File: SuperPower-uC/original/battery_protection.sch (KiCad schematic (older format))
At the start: 0 parts

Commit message: Add "Battery Module" sheet components
+ components libraries
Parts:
- added BT2: 3,7V_18650_LiPo_Bat._Holder, symbol Device:Battery_Cell
- added C8: 100nF, symbol Device:C
- added J9: JST_XH_3A, symbol Connector:Conn_01x02_Male
- added Q6: DMG6968UTS, Package_SO:TSSOP-8_4.4x3mm_P0.65mm, symbol Transistor_FET:DMG6968UTS
- added R21: 330Ohm, symbol Device:R_US
- added R22: 2.7kOhm, symbol Device:R_US
- added U4: AP9101CK6_v2, Package_TO_SOT_SMD:SOT-23-6, symbol Battery_Management:AP9101CK6_v2
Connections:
- net labels added: +BATT, -BATT, GND
- wire segments 0 -> 39
- no-connect marks 0 -> 2
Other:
- note added: "AP9101CK6 Chip price range from Mouser (10/2020) :\n$0.44-0.44 @qt=1\n$0.33-0.33 @qt=10\n$0.17-0.17 @qt=100"
- note added: "AVAILABLE Chips for Lithium-Ion / LiPo or LiFeFO4"
- note added: "Chinese Chip price range from LCSC (10/2020) :\n$0.075-0.115 @qt=10\n$0.054-0.087 @qt=100"
- note added: "Chip + Dual N-Mosfet Version"
- note added: "Compatible pin to pin SOT23-6 ICs List :\n- AP9101CK6 (x65)\n- DW01x (x7)\n- FS312F-G (x1)\n- FS326x (x4)\n- HY2112-xx (x6) for LiFePO4 ONLY\n- HY2113-xxxx (x25) for Lithium ONLY"
- note added: "Compatible pin to pin TSSOP-8 Dual MOSFET List :\n- DMN2019UTS (with ESD Protection diodes)\n- DMG6968UTS (with ESD Protection diodes)\n- FS8205A"
- note added: "Components Price Range"
- note added: "LiFePO4 SOT23-6 ICs List :\n- AP9101CK6-CPTRG1 (3,65V)\n- AP9101CK6-ASTRG1 (3,80V)\n- HY2112-AB (3,75V)\n- HY2112-BB (3,75V)\n- HY2112-CB (3,75V)"
- note added: "LiFePO4 chip list"
- note added: "MOSFET price range from LCSC (10/2020) :\n$0.174-0.357 @qt=1\n$0.128-0.347 @qt=10\n$0.111-0.333 @qt=100"
- note added: "SOT23-6 Package"
- note added: "TSSOP-8 Package"

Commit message: Replace the Dual N-MOSFET by a cheaper version
Replace DMG6968UTS by DMN2019UTS
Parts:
- removed Q6: DMG6968UTS, Package_SO:TSSOP-8_4.4x3mm_P0.65mm, symbol Transistor_FET:DMG6968UTS
- added Q?: DMN2019UTS, Package_SO:TSSOP-8_4.4x3mm_P0.65mm, symbol dmn2019uts:DMN2019UTS
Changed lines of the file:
@@
 	-1   0    0    1
-$EndComp
-$Comp
-L Transistor_FET:DMG6968UTS Q6
-U 1 1 5F79C65E
-P 2650 5200
-F 0 "Q6" H 3094 5196 50  0000 L CNN
-F 1 "DMG6968UTS" H 3094 5105 50  0000 L CNN
-F 2 "Package_SO:TSSOP-8_4.4x3mm_P0.65mm" H 2850 5450 50  0001 L CNN
-F 3 "https://www.diodes.com/assets/Datasheets/ds31793.pdf" H 2450 5200 50  0001 C CNN
-	1    2650 5200
-	1    0    0    -1
 $EndComp
 Wire Wire Line
@@
 Text Label 1050 850  0    50   ~ 0
 +BATT
+$Comp
+L dmn2019uts:DMN2019UTS Q?
+U 1 1 5F864512
+P 2650 5200
+F 0 "Q?" H 3094 5196 50  0000 L CNN
+F 1 "DMN2019UTS" H 3094 5105 50  0000 L CNN
+F 2 "Package_SO:TSSOP-8_4.4x3mm_P0.65mm" H 2850 5450 50  0001 L CNN
+F 3 "https://www.diodes.com/assets/Datasheets/DMN2019UTS.pdf" H 2450 5200 50  0001 C CNN
+	1    2650 5200
+	1    0    0    -1
+$EndComp
 $EndSCHEMATC

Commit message: Add components renaming
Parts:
- gave numbers to parts that had none: 1
- renumbered BT2 to BT1, C8 to C1, J9 to J1, R21 to R1, R22 to R2, U4 to U1
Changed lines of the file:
@@
 VBAT
 $Comp
-L Battery_Management:AP9101CK6_v2 U4
+L Battery_Management:AP9101CK6_v2 U1
 U 1 1 5F786C83
 P 2650 4400
-F 0 "U4" H 2650 4767 50  0000 C CNN
+F 0 "U1" H 2650 4767 50  0000 C CNN
 F 1 "AP9101CK6_v2" H 2650 4676 50  0000 C CNN
 F 2 "Package_TO_SOT_SMD:SOT-23-6" H 2600 4400 50  0001 C CNN
@@
 $EndComp
 $Comp
-L Device:R_US R21
+L Device:R_US R1
 U 1 1 5F78A1A3
 P 1750 4050
-F 0 "R21" H 1818 4096 50  0000 L CNN
+F 0 "R1" H 1818 4096 50  0000 L CNN
 F 1 "330Ohm" H 1818 4005 50  0000 L CNN
 F 2 "" V 1790 4040 50  0001 C CNN
@@
 $EndComp
 $Comp
-L Device:C C8
+L Device:C C1
 U 1 1 5F78A1AD
 P 1750 4550
-F 0 "C8" H 1865 4596 50  0000 L CNN
+F 0 "C1" H 1865 4596 50  0000 L CNN
 F 1 "100nF" H 1865 4505 50  0000 L CNN
 F 2 "" H 1788 4400 50  0001 C CNN
@@
 $EndComp
 $Comp
-L power:GND #PWR031
+L power:GND #PWR05
 U 1 1 5F78A1B7
 P 4000 5000
-F 0 "#PWR031" H 4000 4750 50  0001 C CNN
+F 0 "#PWR05" H 4000 4750 50  0001 C CNN
 F 1 "GND" H 4005 4827 50  0000 C CNN
 F 2 "" H 4000 5000 50  0001 C CNN
@@
 $EndComp
 $Comp
-L Device:R_US R22
+L Device:R_US R2
 U 1 1 5F78A1C1
 P 3500 4550
-F 0 "R22" H 3568 4596 50  0000 L CNN
+F 0 "R2" H 3568 4596 50  0000 L CNN
 F 1 "2.7kOhm" H 3568 4505 50  0000 L CNN
 F 2 "" V 3540 4540 50  0001 C CNN
@@
 	4000 4800 4000 5000
 $Comp
-L power:+BATT #PWR014
+L power:+BATT #PWR01
 U 1 1 5F78A1E8
 P 1750 3700
-F 0 "#PWR014" H 1750 3550 50  0001 C CNN
+F 0 "#PWR01" H 1750 3550 50  0001 C CNN
 F 1 "+BATT" H 1765 3873 50  0000 C CNN
 F 2 "" H 1750 3700 50  0001 C CNN
@@
 $EndComp
 $Comp
-L power:-BATT #PWR028
+L power:-BATT #PWR02
 U 1 1 5F78A1F2
 P 1750 5800
-F 0 "#PWR028" H 1750 5650 50  0001 C CNN
+F 0 "#PWR02" H 1750 5650 50  0001 C CNN
 F 1 "-BATT" H 1765 5973 50  0000 C CNN
 F 2 "" H 1750 5800 50  0001 C CNN
@@
 Compatible pin to pin SOT23-6 ICs List :\n- AP9101CK6 (x65)\n- DW01x (x7)\n- FS312F-G (x1)\n- FS326x (x4)\n- HY2112-xx (x6) for LiFePO4 ONLY\n- HY2113-xxxx (x25) for Lithium ONLY
 $Comp
-L Connector:Conn_01x02_Male J9
+L Connector:Conn_01x02_Male J1
 U 1 1 5F7B2996
 P 2700 1550
-F 0 "J9" H 2808 1731 50  0000 C CNN
+F 0 "J1" H 2808 1731 50  0000 C CNN
 F 1 "JST_XH_3A" H 2650 1650 50  0000 C CNN
 F 2 "" H 2700 1550 50  0001 C CNN
@@
 LiFePO4 SOT23-6 ICs List :\n- AP9101CK6-CPTRG1 (3,65V)\n- AP9101CK6-ASTRG1 (3,80V)\n- HY2112-AB (3,75V)\n- HY2112-BB (3,75V)\n- HY2112-CB (3,75V)
 $Comp
-L Device:Battery_Cell BT2
+L Device:Battery_Cell BT1
 U 1 1 5F7A1B9D
 P 3150 1700
-F 0 "BT2" H 3268 1796 50  0000 L CNN
+F 0 "BT1" H 3268 1796 50  0000 L CNN
 F 1 "3,7V_18650_LiPo_Bat._Holder" H 3268 1705 50  0000 L CNN
 F 2 "" V 3150 1760 50  0001 C CNN
@@
 $EndComp
 $Comp
-L power:-BATT #PWR030
+L power:-BATT #PWR04
 U 1 1 5F7A20F6
 P 3150 2250
-F 0 "#PWR030" H 3150 2100 50  0001 C CNN
+F 0 "#PWR04" H 3150 2100 50  0001 C CNN
 F 1 "-BATT" H 3165 2423 50  0000 C CNN
 F 2 "" H 3150 2250 50  0001 C CNN
@@
 $EndComp
 $Comp
-L power:+BATT #PWR029
+L power:+BATT #PWR03
 U 1 1 5F7A2546
 P 3150 1000
-F 0 "#PWR029" H 3150 850 50  0001 C CNN
+F 0 "#PWR03" H 3150 850 50  0001 C CNN
 F 1 "+BATT" H 3165 1173 50  0000 C CNN
 F 2 "" H 3150 1000 50  0001 C CNN
@@
 +BATT
 $Comp
-L dmn2019uts:DMN2019UTS Q?
+L dmn2019uts:DMN2019UTS Q1
 U 1 1 5F864512
 P 2650 5200
-F 0 "Q?" H 3094 5196 50  0000 L CNN
+F 0 "Q1" H 3094 5196 50  0000 L CNN
 F 1 "DMN2019UTS" H 3094 5105 50  0000 L CNN
 F 2 "Package_SO:TSSOP-8_4.4x3mm_P0.65mm" H 2850 5450 50  0001 L CNN

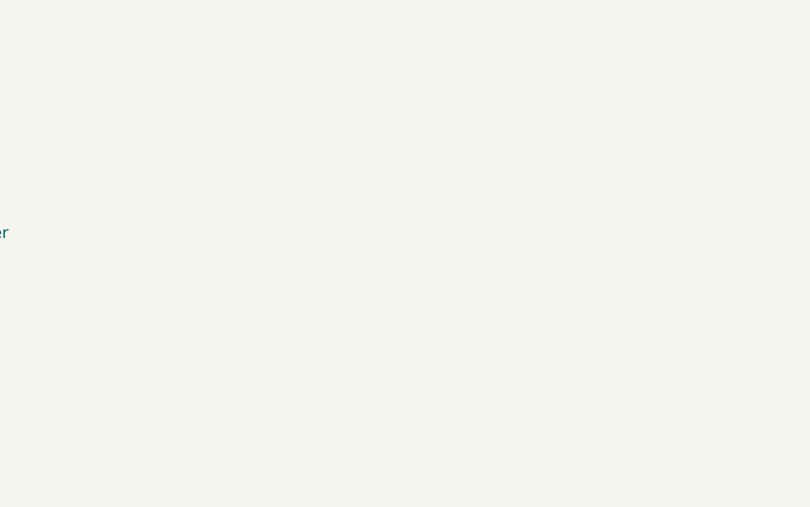
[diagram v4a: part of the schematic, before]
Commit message: Add a "battery protection" bypass 0ohm resistor
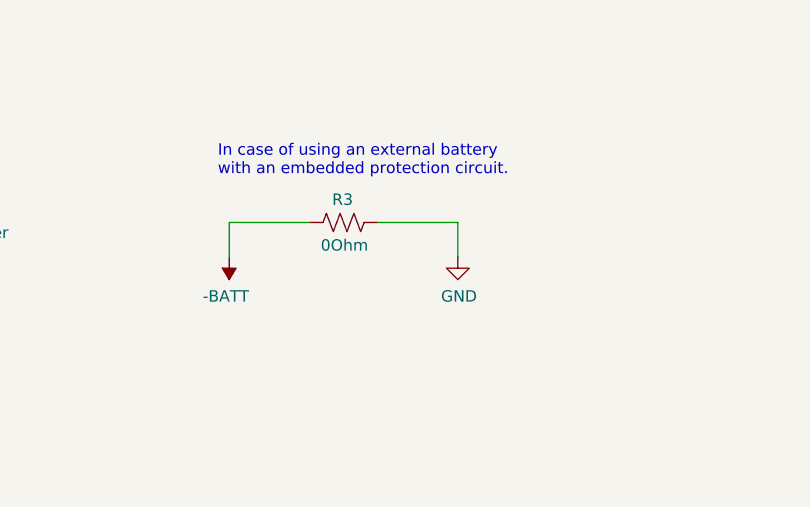
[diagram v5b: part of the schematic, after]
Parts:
- added R3: 0Ohm, symbol Device:R_US
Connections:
- net -BATT: now also R3.2
- net GND: now also R3.1
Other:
- note added: "In case of using an external battery\nwith an embedded protection circuit."
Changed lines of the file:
@@
 	1    0    0    -1
 $EndComp
+$Comp
+L Device:R_US R3
+U 1 1 5F862979
+P 5750 1650
+F 0 "R3" V 5650 1600 50  0000 L CNN
+F 1 "0Ohm" V 5850 1550 50  0000 L CNN
+F 2 "" V 5790 1640 50  0001 C CNN
+F 3 "~" H 5750 1650 50  0001 C CNN
+	1    5750 1650
+	0    1    1    0
+$EndComp
+$Comp
+L power:-BATT #PWR06
+U 1 1 5F863EE5
+P 5250 1800
+F 0 "#PWR06" H 5250 1650 50  0001 C CNN
+F 1 "-BATT" H 5265 1973 50  0000 C CNN
+F 2 "" H 5250 1800 50  0001 C CNN
+F 3 "" H 5250 1800 50  0001 C CNN
+	1    5250 1800
+	-1   0    0    1
+$EndComp
+$Comp
+L power:GND #PWR07
+U 1 1 5F86433E
+P 6250 1800
+F 0 "#PWR07" H 6250 1550 50  0001 C CNN
+F 1 "GND" H 6255 1627 50  0000 C CNN
+F 2 "" H 6250 1800 50  0001 C CNN
+F 3 "" H 6250 1800 50  0001 C CNN
+	1    6250 1800
+	1    0    0    -1
+$EndComp
+Wire Wire Line
+	5250 1800 5250 1650
+Wire Wire Line
+	5250 1650 5600 1650
+Wire Wire Line
+	5900 1650 6250 1650
+Wire Wire Line
+	6250 1650 6250 1800
+Text Notes 5200 1450 0    50   ~ 0
+In case of using an external battery\nwith an embedded protection circuit.
 $EndSCHEMATC

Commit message: Update a symbol library reference -> local
ap9101ck6_v2:AP9101CK6_v2
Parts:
- U1: symbol Battery_Management:AP9101CK6_v2 -> ap9101ck6_v2:AP9101CK6_v2
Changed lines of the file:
@@
 VBAT
 $Comp
-L Battery_Management:AP9101CK6_v2 U1
+L ap9101ck6_v2:AP9101CK6_v2 U1
 U 1 1 5F786C83
 P 2650 4400

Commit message: Try to resolve some DRC
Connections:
- wire segments 43 -> 51
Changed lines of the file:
@@
 Connection ~ 3150 1950
 Wire Wire Line
-	3150 1950 3150 2250
+	3150 1950 3150 2150
 Wire Wire Line
 	2900 1550 2900 1200
@@
 Wire Wire Line
 	3150 1200 3150 1000
-Wire Wire Line
-	1750 3700 1750 3900
 Text Notes 8150 2450 0    50   ~ 0
 Chinese Chip price range from LCSC (10/2020) :\n$0.075-0.115 @qt=10\n$0.054-0.087 @qt=100
@@
 Text Notes 5200 1450 0    50   ~ 0
 In case of using an external battery\nwith an embedded protection circuit.
+$Comp
+L power:PWR_FLAG #FLG0101
+U 1 1 5F8B1179
+P 3500 2250
+F 0 "#FLG0101" H 3500 2325 50  0001 C CNN
+F 1 "PWR_FLAG" H 3500 2423 50  0000 C CNN
+F 2 "" H 3500 2250 50  0001 C CNN
+F 3 "~" H 3500 2250 50  0001 C CNN
+	1    3500 2250
+	-1   0    0    1
+$EndComp
+Wire Wire Line
+	3500 2250 3500 2150
+Wire Wire Line
+	3500 2150 3150 2150
+Connection ~ 3150 2150
+Wire Wire Line
+	3150 2150 3150 2250
+Connection ~ 1750 3800
+Wire Wire Line
+	1750 3800 1750 3900
+Wire Wire Line
+	1750 3700 1750 3800
+Wire Wire Line
+	1400 3800 1750 3800
+Wire Wire Line
+	1400 3700 1400 3800
+$Comp
+L power:PWR_FLAG #FLG0102
+U 1 1 5F8B2D96
+P 1400 3700
+F 0 "#FLG0102" H 1400 3775 50  0001 C CNN
+F 1 "PWR_FLAG" H 1400 3873 50  0000 C CNN
+F 2 "" H 1400 3700 50  0001 C CNN
+F 3 "~" H 1400 3700 50  0001 C CNN
+	1    1400 3700
+	1    0    0    -1
+$EndComp
+Wire Wire Line
+	1400 4300 1750 4300
+Wire Wire Line
+	1400 4200 1400 4300
+$Comp
+L power:PWR_FLAG #FLG0103
+U 1 1 5F8B93BE
+P 1400 4200
+F 0 "#FLG0103" H 1400 4275 50  0001 C CNN
+F 1 "PWR_FLAG" H 1400 4373 50  0000 C CNN
+F 2 "" H 1400 4200 50  0001 C CNN
+F 3 "~" H 1400 4200 50  0001 C CNN
+	1    1400 4200
+	1    0    0    -1
+$EndComp
 $EndSCHEMATC

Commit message: Cleanup schematics
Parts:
- R1, R2: symbol Device:R_US -> Device:R
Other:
- moved on the sheet: BT1, J1
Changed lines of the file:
@@
 $EndComp
 $Comp
-L Device:R_US R1
+L Device:R R1
 U 1 1 5F78A1A3
 P 1750 4050
@@
 L power:GND #PWR05
 U 1 1 5F78A1B7
-P 4000 5000
-F 0 "#PWR05" H 4000 4750 50  0001 C CNN
-F 1 "GND" H 4005 4827 50  0000 C CNN
-F 2 "" H 4000 5000 50  0001 C CNN
-F 3 "" H 4000 5000 50  0001 C CNN
-	1    4000 5000
-	1    0    0    -1
-$EndComp
-$Comp
-L Device:R_US R2
+P 3500 5750
+F 0 "#PWR05" H 3500 5500 50  0001 C CNN
+F 1 "GND" H 3505 5577 50  0000 C CNN
+F 2 "" H 3500 5750 50  0001 C CNN
+F 3 "" H 3500 5750 50  0001 C CNN
+	1    3500 5750
+	1    0    0    -1
+$EndComp
+$Comp
+L Device:R R2
 U 1 1 5F78A1C1
 P 3500 4550
@@
 	2750 4700 2750 4800
 Wire Wire Line
-	3500 4800 3500 4700
-Wire Wire Line
 	1750 4200 1750 4300
 Wire Wire Line
@@
 	1750 4300 1750 4400
 Connection ~ 1750 4800
-Wire Wire Line
-	3500 4800 4000 4800
-Wire Wire Line
-	4000 4800 4000 5000
 $Comp
 L power:+BATT #PWR01
@@
 	2900 5550 3500 5550
 Wire Wire Line
-	3500 5550 3500 4800
-Connection ~ 3500 4800
-Wire Wire Line
 	2550 5550 2550 5650
 Wire Wire Line
@@
 Text Notes 2350 4000 0    50   ~ 0
 SOT23-6 Package
-Text Notes 3100 5450 0    50   ~ 0
+Text Notes 2300 4900 0    50   ~ 0
 TSSOP-8 Package
 Text Notes 4400 4550 0    50   ~ 0
@@
 L Connector:Conn_01x02_Male J1
 U 1 1 5F7B2996
-P 2700 1550
-F 0 "J1" H 2808 1731 50  0000 C CNN
-F 1 "JST_XH_3A" H 2650 1650 50  0000 C CNN
-F 2 "" H 2700 1550 50  0001 C CNN
-F 3 "~" H 2700 1550 50  0001 C CNN
-	1    2700 1550
+P 2650 1550
+F 0 "J1" H 2758 1731 50  0000 C CNN
+F 1 "JST_XH_3A" H 2600 1650 50  0000 C CNN
+F 2 "" H 2650 1550 50  0001 C CNN
+F 3 "~" H 2650 1550 50  0001 C CNN
+	1    2650 1550
 	1    0    0    -1
 $EndComp
@@
 Text Notes 8150 2100 0    50   ~ 0
 AP9101CK6 Chip price range from Mouser (10/2020) :\n$0.44-0.44 @qt=1\n$0.33-0.33 @qt=10\n$0.17-0.17 @qt=100
-Text Notes 4400 6050 0    50   ~ 0
+Text Notes 4400 6150 0    50   ~ 0
 Compatible pin to pin TSSOP-8 Dual MOSFET List :\n- DMN2019UTS (with ESD Protection diodes)\n- DMG6968UTS (with ESD Protection diodes)\n- FS8205A
 Text Notes 8150 3300 0    50   ~ 0
@@
 L Device:Battery_Cell BT1
 U 1 1 5F7A1B9D
-P 3150 1700
-F 0 "BT1" H 3268 1796 50  0000 L CNN
-F 1 "3,7V_18650_LiPo_Bat._Holder" H 3268 1705 50  0000 L CNN
-F 2 "" V 3150 1760 50  0001 C CNN
-F 3 "~" V 3150 1760 50  0001 C CNN
-	1    3150 1700
+P 3150 1650
+F 0 "BT1" H 3268 1746 50  0000 L CNN
+F 1 "3,7V_18650_LiPo_Bat._Holder" H 3268 1655 50  0000 L CNN
+F 2 "" V 3150 1710 50  0001 C CNN
+F 3 "~" V 3150 1710 50  0001 C CNN
+	1    3150 1650
 	1    0    0    -1
 $EndComp
@@
 L power:-BATT #PWR04
 U 1 1 5F7A20F6
-P 3150 2250
-F 0 "#PWR04" H 3150 2100 50  0001 C CNN
-F 1 "-BATT" H 3165 2423 50  0000 C CNN
-F 2 "" H 3150 2250 50  0001 C CNN
-F 3 "" H 3150 2250 50  0001 C CNN
-	1    3150 2250
+P 3150 2050
+F 0 "#PWR04" H 3150 1900 50  0001 C CNN
+F 1 "-BATT" H 3165 2223 50  0000 C CNN
+F 2 "" H 3150 2050 50  0001 C CNN
+F 3 "" H 3150 2050 50  0001 C CNN
+	1    3150 2050
 	-1   0    0    1
 $EndComp
@@
 L power:+BATT #PWR03
 U 1 1 5F7A2546
-P 3150 1000
-F 0 "#PWR03" H 3150 850 50  0001 C CNN
-F 1 "+BATT" H 3165 1173 50  0000 C CNN
-F 2 "" H 3150 1000 50  0001 C CNN
-F 3 "" H 3150 1000 50  0001 C CNN
-	1    3150 1000
-	1    0    0    -1
-$EndComp
-Wire Wire Line
-	3150 1500 3150 1200
-Wire Wire Line
-	3150 1800 3150 1950
-Wire Wire Line
-	2900 1650 2900 1950
-Wire Wire Line
-	2900 1950 3150 1950
-Connection ~ 3150 1950
-Wire Wire Line
-	3150 1950 3150 2150
-Wire Wire Line
-	2900 1550 2900 1200
-Wire Wire Line
-	2900 1200 3150 1200
-Connection ~ 3150 1200
-Wire Wire Line
-	3150 1200 3150 1000
+P 3150 1250
+F 0 "#PWR03" H 3150 1100 50  0001 C CNN
+F 1 "+BATT" H 3165 1423 50  0000 C CNN
+F 2 "" H 3150 1250 50  0001 C CNN
+F 3 "" H 3150 1250 50  0001 C CNN
+	1    3150 1250
+	1    0    0    -1
+$EndComp
+Wire Wire Line
+	3150 1450 3150 1350
+Wire Wire Line
+	3150 1750 3150 1850
+Wire Wire Line
+	2950 1650 2950 1850
+Wire Wire Line
+	2950 1850 3150 1850
+Wire Wire Line
+	3150 1850 3150 1950
+Wire Wire Line
+	2950 1550 2950 1350
+Wire Wire Line
+	2950 1350 3150 1350
+Connection ~ 3150 1350
+Wire Wire Line
+	3150 1350 3150 1250
 Text Notes 8150 2450 0    50   ~ 0
 Chinese Chip price range from LCSC (10/2020) :\n$0.075-0.115 @qt=10\n$0.054-0.087 @qt=100
@@
 	8200 5550 8200 4750
 Wire Notes Line
-	4300 5950 2650 5950
-Wire Notes Line
-	2650 5950 2650 5600
+	4300 6050 2650 6050
+Wire Notes Line
+	2650 6050 2650 5700
 Wire Notes Line
 	3050 4200 4350 4200
@@
 P 2650 5200
 F 0 "Q1" H 3094 5196 50  0000 L CNN
-F 1 "DMN2019UTS" H 3094 5105 50  0000 L CNN
+F 1 "DMN2019UTS" H 3000 5050 50  0000 L CNN
 F 2 "Package_SO:TSSOP-8_4.4x3mm_P0.65mm" H 2850 5450 50  0001 L CNN
 F 3 "https://www.diodes.com/assets/Datasheets/DMN2019UTS.pdf" H 2450 5200 50  0001 C CNN
@@
 L power:-BATT #PWR06
 U 1 1 5F863EE5
-P 5250 1800
-F 0 "#PWR06" H 5250 1650 50  0001 C CNN
-F 1 "-BATT" H 5265 1973 50  0000 C CNN
-F 2 "" H 5250 1800 50  0001 C CNN
-F 3 "" H 5250 1800 50  0001 C CNN
-	1    5250 1800
+P 5500 1750
+F 0 "#PWR06" H 5500 1600 50  0001 C CNN
+F 1 "-BATT" H 5515 1923 50  0000 C CNN
+F 2 "" H 5500 1750 50  0001 C CNN
+F 3 "" H 5500 1750 50  0001 C CNN
+	1    5500 1750
 	-1   0    0    1
 $EndComp
@@
 L power:GND #PWR07
 U 1 1 5F86433E
-P 6250 1800
-F 0 "#PWR07" H 6250 1550 50  0001 C CNN
-F 1 "GND" H 6255 1627 50  0000 C CNN
-F 2 "" H 6250 1800 50  0001 C CNN
-F 3 "" H 6250 1800 50  0001 C CNN
-	1    6250 1800
-	1    0    0    -1
-$EndComp
-Wire Wire Line
-	5250 1800 5250 1650
-Wire Wire Line
-	5250 1650 5600 1650
-Wire Wire Line
-	5900 1650 6250 1650
-Wire Wire Line
-	6250 1650 6250 1800
+P 6000 1750
+F 0 "#PWR07" H 6000 1500 50  0001 C CNN
+F 1 "GND" H 6005 1577 50  0000 C CNN
+F 2 "" H 6000 1750 50  0001 C CNN
+F 3 "" H 6000 1750 50  0001 C CNN
+	1    6000 1750
+	1    0    0    -1
+$EndComp
+Wire Wire Line
+	5500 1750 5500 1650
+Wire Wire Line
+	5500 1650 5600 1650
+Wire Wire Line
+	5900 1650 6000 1650
+Wire Wire Line
+	6000 1650 6000 1750
 Text Notes 5200 1450 0    50   ~ 0
 In case of using an external battery\nwith an embedded protection circuit.
@@
 L power:PWR_FLAG #FLG0101
 U 1 1 5F8B1179
-P 3500 2250
-F 0 "#FLG0101" H 3500 2325 50  0001 C CNN
-F 1 "PWR_FLAG" H 3500 2423 50  0000 C CNN
-F 2 "" H 3500 2250 50  0001 C CNN
-F 3 "~" H 3500 2250 50  0001 C CNN
-	1    3500 2250
+P 3500 2050
+F 0 "#FLG0101" H 3500 2125 50  0001 C CNN
+F 1 "PWR_FLAG" H 3500 2223 50  0000 C CNN
+F 2 "" H 3500 2050 50  0001 C CNN
+F 3 "~" H 3500 2050 50  0001 C CNN
+	1    3500 2050
 	-1   0    0    1
 $EndComp
 Wire Wire Line
-	3500 2250 3500 2150
-Wire Wire Line
-	3500 2150 3150 2150
-Connection ~ 3150 2150
-Wire Wire Line
-	3150 2150 3150 2250
+	3500 2050 3500 1950
+Wire Wire Line
+	3500 1950 3150 1950
+Connection ~ 3150 1950
+Wire Wire Line
+	3150 1950 3150 2050
 Connection ~ 1750 3800
 Wire Wire Line
@@
 	1    0    0    -1
 $EndComp
+Wire Wire Line
+	3500 4700 3500 5550
+Wire Wire Line
+	3500 5650 3500 5750
+Connection ~ 3500 5650
+Wire Wire Line
+	2850 1550 2950 1550
+Wire Wire Line
+	2950 1650 2850 1650
+Connection ~ 3150 1850
 $EndSCHEMATC
